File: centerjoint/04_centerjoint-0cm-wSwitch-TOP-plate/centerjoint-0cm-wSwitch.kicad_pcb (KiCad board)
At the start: 2 copper layers, 79.1 x 48.4 mm, 12 parts

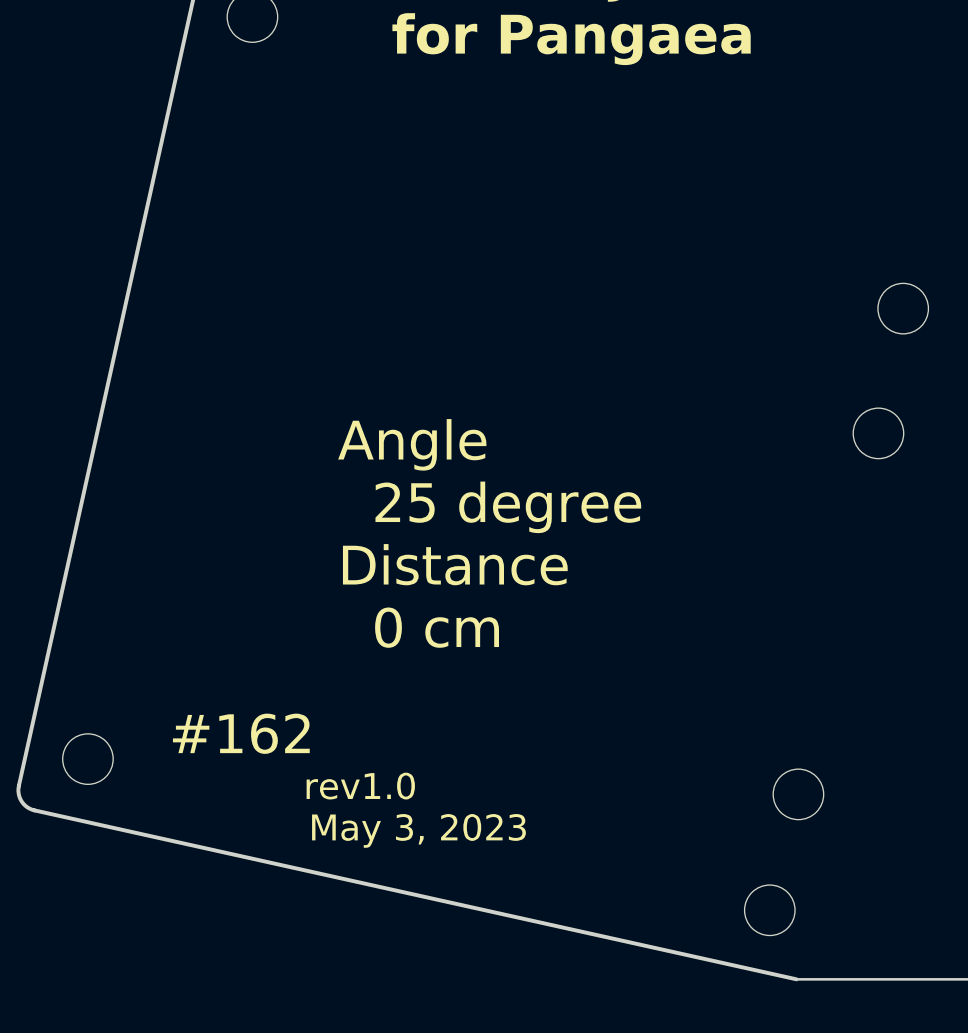
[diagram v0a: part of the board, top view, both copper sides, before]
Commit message: removed unnecessary files.
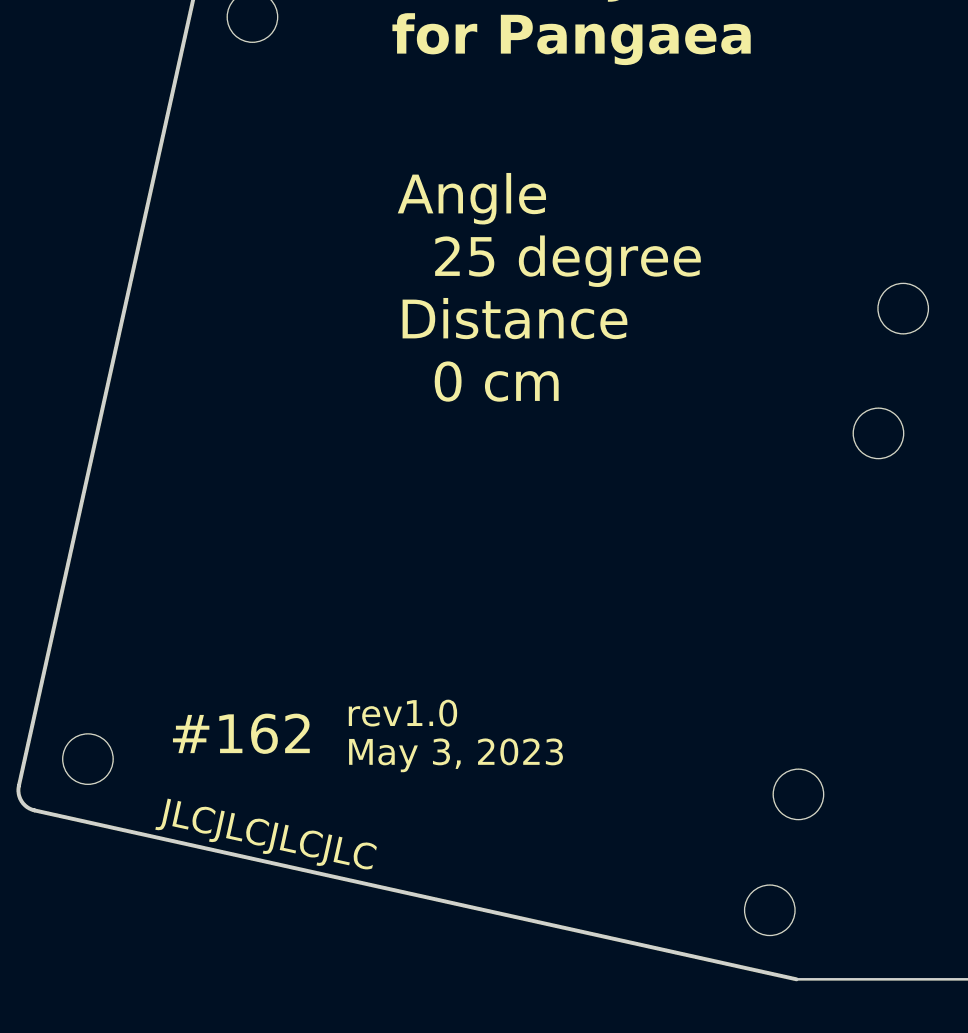
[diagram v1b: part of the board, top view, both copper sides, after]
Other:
- board text added: "JLCJLCJLCJLC"
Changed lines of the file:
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@@
   (gr_line (start 46.426617 62.666585) (end 16.979087 56.138224)
     (stroke (width 0.15) (type solid)) (layer "Edge.Cuts"))
+  (gr_text "JLCJLCJLCJLC" (at 21.75 56.75 347.5) (layer "F.SilkS")
+    (effects (font (size 1 1) (thickness 0.15)) (justify left bottom))
+  )
   (gr_text "Center Joint\nfor Pangaea" (at 30.769984 27.079998) (layer "F.SilkS")
     (effects (font (size 1.5 1.5) (thickness 0.25) bold) (justify left bottom))
   )
-  (gr_text "rev1.0" (at 27.369984 55.819771) (layer "F.SilkS")
+  (gr_text "rev1.0" (at 29 53) (layer "F.SilkS")
     (effects (font (size 1 1) (thickness 0.15)) (justify left bottom))
   )
-  (gr_text "May 3, 2023" (at 27.569984 57.419771) (layer "F.SilkS")
+  (gr_text "May 3, 2023" (at 29 54.5) (layer "F.SilkS")
     (effects (font (size 1 1) (thickness 0.15)) (justify left bottom))
   )
-  (gr_text "Angle\n  25 degree\nDistance\n  0 cm" (at 28.695747 50.009998) (layer "F.SilkS")
+  (gr_text "Angle\n  25 degree\nDistance\n  0 cm" (at 31 40.5) (layer "F.SilkS")
     (effects (font (size 1.5 1.5) (thickness 0.15)) (justify left bottom))
   )
